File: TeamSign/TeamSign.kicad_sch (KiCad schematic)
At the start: 59 parts, among them J1 RJ45, U1 TPS563200, U2 ESP32-Devkit_C_V4

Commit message: Add SK6812-Side-A footprint/symbol to working area, as well as swapped to a stacklight connection that has a ground pin at the end for generic 12v power use.  yay!
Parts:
- L1: value L -> 3.3uH; footprint (none) -> Inductor_SMD:L_Bourns_SRN8040TA; LCSC (none) -> https://www.lcsc.com/product-detail/Power-Inductors_BOURNS-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
- R1: value 56.2kOhm -> 56.2kΩ
- R2: value 10kOhm -> 10kΩ
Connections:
- net +12V: now also J1.1
- net GND: now also J1.8
- net sk_input: now reaches U2.26 (RTC_GPIO9/XTal32P/Touch9/ADC1_4/GPIO32)
- net sk_input: now also D1.2 (DIN)
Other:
- moved on the sheet: J1
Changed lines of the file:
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@@
+    (stroke (width 0) (type default))
+  )
+  (wire (pts (xy 22.225 95.25) (xy 24.765 95.25))
     (stroke (width 0) (type default))
   )
@@
     (stroke (width 0) (type default))
   )
+  (wire (pts (xy 157.48 113.665) (xy 167.005 113.665))
+    (stroke (width 0) (type default))
+  )
   (wire (pts (xy 223.52 255.905) (xy 234.95 255.905))
     (stroke (width 0) (type default))
@@
     (stroke (width 0) (type default))
   )
+  (wire (pts (xy 22.225 113.03) (xy 24.765 113.03))
+    (stroke (width 0) (type default))
+  )
   (wire (pts (xy 264.16 255.905) (xy 275.59 255.905))
     (stroke (width 0) (type default))
@@
   )
   (wire (pts (xy 223.52 274.32) (xy 234.95 274.32))
+    (stroke (width 0) (type default))
+  )
+  (wire (pts (xy 25.4 238.125) (xy 35.56 238.125))
     (stroke (width 0) (type default))
   )
@@
     (effects (font (size 1.27 1.27)) (justify left bottom))
   )
+  (label "sk_input" (at 157.48 113.665 0) (fields_autoplaced)
+    (effects (font (size 1.27 1.27)) (justify left bottom))
+  )
+  (label "sk_input" (at 25.4 238.125 0) (fields_autoplaced)
+    (effects (font (size 1.27 1.27)) (justify left bottom))
+  )
   (symbol (lib_id "LED:SK6812") (at 214.63 266.7 0) (unit 1)
     (in_bom yes) (on_board yes) (dnp no)
@@
       (effects (font (size 1.27 1.27)) (justify left))
     )
-    (property "Value" "10kOhm" (at 81.28 66.675 0)
+    (property "Value" "10kΩ" (at 81.28 66.675 0)
       (effects (font (size 1.27 1.27)) (justify left))
     )
@@
     )
   )
-  (symbol (lib_id "Connector:RJ45") (at 30.48 107.95 0) (unit 1)
-    (in_bom yes) (on_board yes) (dnp no) (fields_autoplaced)
-    (property "Reference" "J1" (at 30.48 90.805 0)
-      (effects (font (size 1.27 1.27)))
-    )
-    (property "Value" "RJ45" (at 30.48 93.345 0)
-      (effects (font (size 1.27 1.27)))
-    )
-    (property "Footprint" "footprints:RCH RC00139" (at 30.48 107.315 90)
-      (effects (font (size 1.27 1.27)) hide)
-    )
-    (property "Datasheet" "~" (at 30.48 107.315 90)
+  (symbol (lib_id "Connector:RJ45") (at 34.925 102.87 180) (unit 1)
+    (in_bom yes) (on_board yes) (dnp no) (fields_autoplaced)
+    (property "Reference" "J1" (at 44.45 103.505 0)
+      (effects (font (size 1.27 1.27)) (justify right))
+    )
+    (property "Value" "RJ45" (at 44.45 106.045 0)
+      (effects (font (size 1.27 1.27)) (justify right))
+    )
+    (property "Footprint" "footprints:RCH RC00139" (at 34.925 103.505 90)
+      (effects (font (size 1.27 1.27)) hide)
+    )
+    (property "Datasheet" "~" (at 34.925 103.505 90)
       (effects (font (size 1.27 1.27)) hide)
     )
@@
       (effects (font (size 1.27 1.27)))
     )
-    (property "Value" "L" (at 86.36 52.705 90)
-      (effects (font (size 1.27 1.27)))
-    )
-    (property "Footprint" "" (at 86.36 54.61 0)
-      (effects (font (size 1.27 1.27)) hide)
-    )
-    (property "Datasheet" "~" (at 86.36 54.61 0)
+    (property "Value" "3.3uH" (at 86.36 52.705 90)
+      (effects (font (size 1.27 1.27)))
+    )
+    (property "Footprint" "Inductor_SMD:L_Bourns_SRN8040TA" (at 86.36 54.61 0)
+      (effects (font (size 1.27 1.27)) hide)
+    )
+    (property "Datasheet" "https://datasheet.lcsc.com/lcsc/2012151538_BOURNS-SRN8040-3R3Y_C780188.pdf" (at 86.36 54.61 0)
+      (effects (font (size 1.27 1.27)) hide)
+    )
+    (property "LCSC" "https://www.lcsc.com/product-detail/Power-Inductors_BOURNS-SRN8040-3R3Y_C780188.html" (at 86.36 54.61 90)
       (effects (font (size 1.27 1.27)) hide)
     )
@@
       (effects (font (size 1.27 1.27)) (justify left))
     )
-    (property "Value" "56.2kOhm" (at 80.01 60.96 0)
+    (property "Value" "56.2kΩ" (at 80.01 60.96 0)
       (effects (font (size 1.27 1.27)) (justify left))
     )
@@
         (path "/e53f9913-0070-41c4-b6c8-5a044462b6d9"
           (reference "D7") (unit 1)
+        )
+      )
+    )
+  )
+  (symbol (lib_id "power:+12V") (at 22.225 95.25 0) (unit 1)
+    (in_bom yes) (on_board yes) (dnp no) (fields_autoplaced)
+    (property "Reference" "#PWR010" (at 22.225 99.06 0)
+      (effects (font (size 1.27 1.27)) hide)
+    )
+    (property "Value" "+12V" (at 22.225 91.44 0)
+      (effects (font (size 1.27 1.27)))
+    )
+    (property "Footprint" "" (at 22.225 95.25 0)
+      (effects (font (size 1.27 1.27)) hide)
+    )
+    (property "Datasheet" "" (at 22.225 95.25 0)
+      (effects (font (size 1.27 1.27)) hide)
+    )
+    (pin "1")
+    (instances
+      (project "TeamSign"
+        (path "/e53f9913-0070-41c4-b6c8-5a044462b6d9"
+          (reference "#PWR010") (unit 1)
         )
       )
@@
         )
       )
+    )
+  )
+  (symbol (lib_id "power:GND") (at 22.225 113.03 0) (unit 1)
+    (in_bom yes) (on_board yes) (dnp no) (fields_autoplaced)
+    (property "Reference" "#PWR011" (at 22.225 119.38 0)
+      (effects (font (size 1.27 1.27)) hide)
+    )
+    (property "Value" "GND" (at 22.225 117.475 0)
+      (effects (font (size 1.27 1.27)))
+    )
+    (property "Footprint" "" (at 22.225 113.03 0)
+      (effects (font (size 1.27 1.27)) hide)
+    )
+    (property "Datasheet" "" (at 22.225 113.03 0)
+      (effects (font (size 1.27 1.27)) hide)
+    )
+    (pin "1")
+    (instances
+      (project "TeamSign"
+        (path "/e53f9913-0070-41c4-b6c8-5a044462b6d9"
+          (reference "#PWR011") (unit 1)
+        )
+      )

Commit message: Added subsheet for the other LEDs, still need to fix the capacitor footprint, but making solid progress it seems?  Wild!
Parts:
- removed C10, C11, C12, C13, C14, C15, C16, C17, C18, C19, C20, C21, C22, C23, C24, C25, C26, C27, C28, C4, C5, C6, C7, C8, C9: C, symbol Device:C
- removed D1, D10, D11, D12, D13, D14, D15, D16, D17, D18, D19, D2, D20, D21, D22, D23, D24, D25, D3, D4, D5, D6, D7, D8, D9: SK6812, LED_SMD:LED_SK6812_PLCC4_5.0x5.0mm_P3.2mm, symbol LED:SK6812
- added C29, C30, C31, C32, C33, C34, C35, C36: C, symbol Device:C
- added D26, D27, D28, D29, D30, D31, D32, D33: SK6812-Side-A, footprints:SK6812-Side-A, symbol symbols:SK6812_Side_A
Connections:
- net +3V3: now also C29.1, C30.1, C31.1, C32.1, C33.1, C34.1, C35.1, C36.1, D26.2 (VDD), D27.2 (VDD), D28.2 (VDD), D29.2 (VDD), D30.2 (VDD), D31.2 (VDD), D32.2 (VDD), D33.2 (VDD); no longer C3.1, L1.2, R1.1, U2.20 (3.3v)
- net GND: now also C29.2, C30.2, C31.2, C32.2, C33.2, C34.2, C35.2, C36.2, D26.4 (GND), D27.4 (GND), D28.4 (GND), D29.4 (GND), D30.4 (GND), D31.4 (GND), D32.4 (GND), D33.4 (GND)
- net stacklight_out: now reaches U2.27 (RTC_GPIO8/Xtal32N/Touch8/ADC1_5/GPIO33)
- net stacklight_out: now also D26.1 (DIN)
- net +5V: now reaches U2.38 (5V)
- net +5V: now also C3.1, L1.2, R1.1
- new net: D32.3 (DOUT), D33.1 (DIN)
- new net: D31.3 (DOUT), D32.1 (DIN)
- new net: D29.3 (DOUT), D30.1 (DIN)
- new net: D30.3 (DOUT), D31.1 (DIN)
- new net: D28.3 (DOUT), D29.1 (DIN)
- new net: D26.3 (DOUT), D27.1 (DIN)
- new net: D27.3 (DOUT), D28.1 (DIN)
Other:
- added sheet LED Array 1 (LED_Array_1.kicad_sch)
- added sheet LED Array 2 (LED_Array_1.kicad_sch)
- added sheet LED Array 3 (LED_Array_1.kicad_sch)
- note removed: "DID NO ONE ELSE SERIOUSLY WANT THIS‽"
- note removed: "MAKE SIDE FIRING SK6812 SIDE A FOOTPRINT FUCKING FUCKING FUCK!"
- note removed: "SK6812 Output (7Seg)"

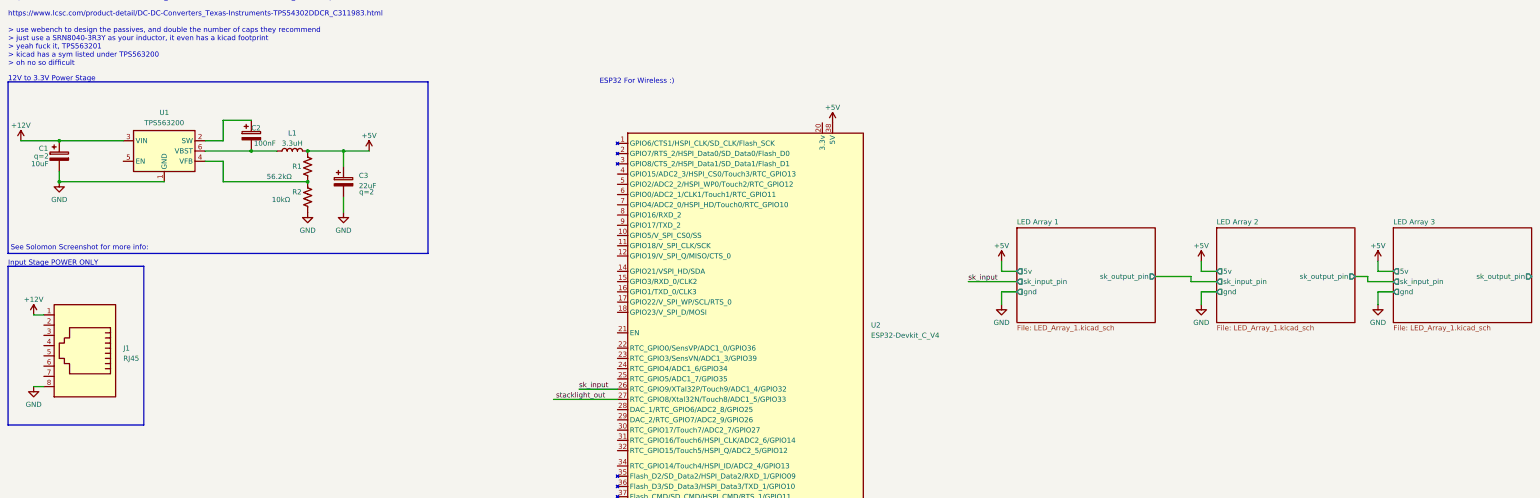
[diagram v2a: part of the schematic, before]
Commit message: Add PEM nut footprint starter to library, also did small tweaks to BOM and updated symbols to include the barrel jack antics.  Yay!
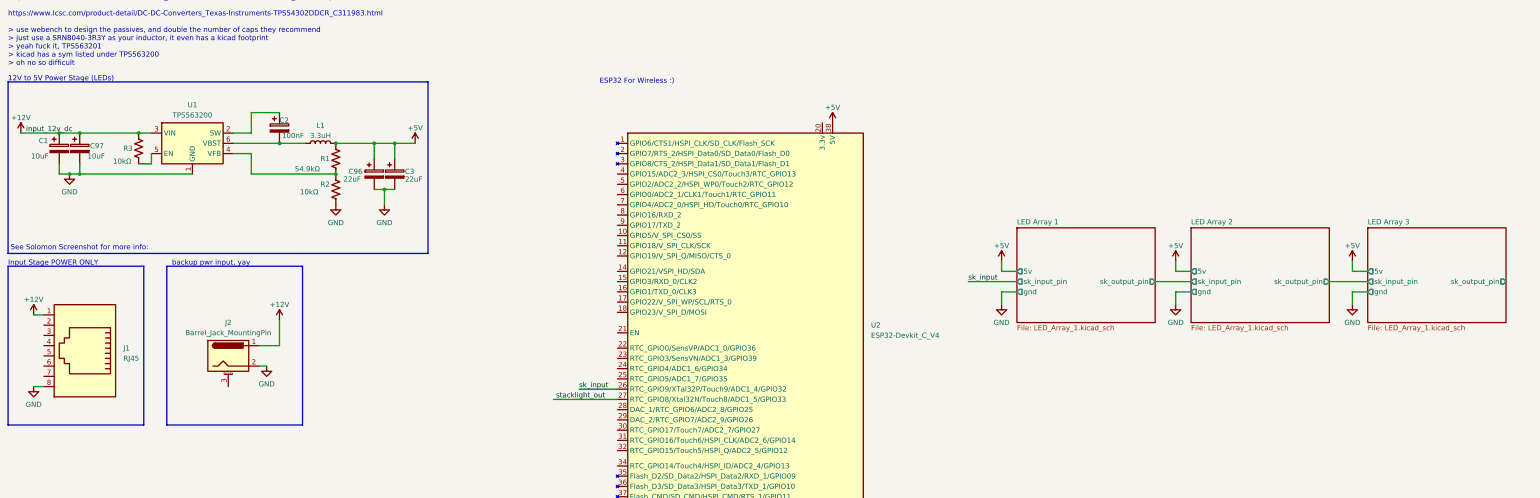
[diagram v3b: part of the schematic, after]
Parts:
- added C96: 22uF, Capacitor_SMD:CP_Elec_5x5.4, symbol Device:C_Polarized
- added C97: 10uF, Capacitor_SMD:C_1206_3216Metric_Pad1.33x1.80mm_HandSolder, symbol Device:C_Polarized
- added J2: Barrel_Jack_MountingPin, Connector_BarrelJack:BarrelJack_Horizontal, symbol symbols:Barrel_Jack_MountingPin
- added R3: 10kΩ, Resistor_SMD:R_0805_2012Metric_Pad1.20x1.40mm_HandSolder, symbol Device:R_US
- C1: footprint (none) -> Capacitor_SMD:C_1206_3216Metric_Pad1.33x1.80mm_HandSolder; LCSC (none) -> https://www.lcsc.com/product-detail/Multilayer-Ceramic-Capa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; Quantity q=2 -> (none)
- C2: footprint (none) -> Capacitor_SMD:C_1206_3216Metric_Pad1.33x1.80mm_HandSolder; LCSC (none) -> https://www.lcsc.com/product-detail/Multilayer-Ceramic-Capa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
- C3: footprint (none) -> Capacitor_SMD:CP_Elec_5x5.4; LCSC (none) -> https://www.lcsc.com/product-detail/Aluminum-Electrolytic-C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; Quantity q=2 -> (none)
- R1: value 56.2kΩ -> 54.9kΩ; footprint (none) -> Resistor_SMD:R_0805_2012Metric_Pad1.20x1.40mm_HandSolder; LCSC (none) -> https://www.lcsc.com/product-detail/Chip-Resistor-Surface-M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
- R2: footprint (none) -> Resistor_SMD:R_0805_2012Metric_Pad1.20x1.40mm_HandSolder; LCSC (none) -> https://www.lcsc.com/product-detail/Chip-Resistor-Surface-M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
- U1: Note (none) -> This is actually a TPS563201, but we're using the footprint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
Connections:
- net +12V: now also C97.1, J2.1, R3.1
- net +5V: now also C96.1
- net GND: now also C96.2, C97.2, J2.2
- net at U1.5 (EN): now also R3.2
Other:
- note added: "12V to 5V Power Stage (LEDs)"
- note added: "backup pwr input, yay"
- note removed: "12V to 3.3V Power Stage"
- moved on the sheet: C1, C2, C3, L1, R1, R2, U1

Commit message: Place caps :)
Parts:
- added C98: 100nF, Capacitor_SMD:C_1206_3216Metric_Pad1.33x1.80mm_HandSolder, symbol Device:C
- C29, C30, C31, C32, C33, C34, C35, C36: value C -> 100nF; footprint (none) -> Capacitor_SMD:C_1206_3216Metric_Pad1.33x1.80mm_HandSolder; LCSC (none) -> https://www.lcsc.com/product-detail/Multilayer-Ceramic-Capa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
- renumbered C2 to C799, C96 to C898, C3 to C899, C97 to C998, C1 to C999, D26 to D300, D27 to D301, D28 to D302, D29 to D303, D30 to D304, D31 to D305, D32 to D306, D33 to D307
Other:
- note added: "ESP32! Yay!"
- note added: "LED Arrays"
- note removed: "ESP32 For Wireless :)"
- moved on the sheet: U2

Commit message: Added gerbers for TS to the ignore, plus added level shifting.  Yay!
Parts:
- added Q1, Q2: BSS138, Package_TO_SOT_SMD:SOT-23, symbol Transistor_FET:BSS138
- added R4, R5, R6, R7: 10kΩ, Resistor_SMD:R_0805_2012Metric_Pad1.20x1.40mm_HandSolder, symbol Device:R_US
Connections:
- net +5V: now also R5.1, R7.1
- net sk_input: now also Q1.2 (S), R4.2
- net stacklight_out: now also Q2.2 (S), R6.2; no longer D300.1 (DIN)
- net +3.3V: now reaches U2.20 (3.3v)
- net +3.3V: now also Q1.1 (G), Q2.1 (G), R4.1, R6.1
- new net sk_lvl_shifted: Q1.3 (D), R5.2
- new net stacklight_lvl_shift: D300.1 (DIN), Q2.3 (D), R7.2
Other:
- note added: "Level Shifting for SK6812 Variants"
- note added: "Stacklight Emulation Mode Shit"
- moved on the sheet: C29, C30, C31, C32, C33, C34, C35, C36, C98, D300, D301, D302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

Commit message: Resolve subsheet antics... Yay.
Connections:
- net +3V3 is gone; now on net +5V: C29.1, C30.1, C31.1, C32.1, C33.1, C34.1, C35.1, C36.1, D300.2 (VDD), D301.2 (VDD), D302.2 (VDD), D303.2 (VDD), D304.2 (VDD), D305.2 (VDD), D306.2 (VDD), D307.2 (VDD)
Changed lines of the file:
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@@
-    )
-  )
-  (symbol (lib_id "power:+3V3") (at 208.28 144.145 0) (unit 1)
-    (in_bom yes) (on_board yes) (dnp no) (fields_autoplaced)
-    (property "Reference" "#PWR017" (at 208.28 147.955 0)
-      (effects (font (size 1.27 1.27)) hide)
-    )
-    (property "Value" "+3V3" (at 208.28 140.335 0)
-      (effects (font (size 1.27 1.27)))
-    )
-    (property "Footprint" "" (at 208.28 144.145 0)
-      (effects (font (size 1.27 1.27)) hide)
-    )
-    (property "Datasheet" "" (at 208.28 144.145 0)
-      (effects (font (size 1.27 1.27)) hide)
-    )
-    (pin "1")
-    (instances
-      (project "TeamSign"
-        (path "/e53f9913-0070-41c4-b6c8-5a044462b6d9"
-          (reference "#PWR017") (unit 1)
-        )
-      )
     )
   )
@@
         )
       )
+    )
+  )
+  (symbol (lib_id "power:+5V") (at 208.28 144.145 0) (unit 1)
+    (in_bom yes) (on_board yes) (dnp no) (fields_autoplaced)
+    (property "Reference" "#PWR017" (at 208.28 147.955 0)
+      (effects (font (size 1.27 1.27)) hide)
+    )
+    (property "Value" "+5V" (at 208.28 140.335 0)
+      (effects (font (size 1.27 1.27)))
+    )
+    (property "Footprint" "" (at 208.28 144.145 0)
+      (effects (font (size 1.27 1.27)) hide)
+    )
+    (property "Datasheet" "" (at 208.28 144.145 0)
+      (effects (font (size 1.27 1.27)) hide)
+    )
+    (pin "1")
+    (instances
+      (project "TeamSign"
+        (path "/e53f9913-0070-41c4-b6c8-5a044462b6d9"
+          (reference "#PWR017") (unit 1)
+        )
+      )

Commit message: Added power area, and started drawing pours.
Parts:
- added C87, C90, C93, C96: 100nF, Capacitor_SMD:C_1206_3216Metric_Pad1.33x1.80mm_HandSolder, symbol Device:C
- added D29, D30, D31, D32: SK6812, LED_SMD:LED_SK6812_PLCC4_5.0x5.0mm_P3.2mm, symbol LED:SK6812
- added H1, H2, H3, H4: MountingHole, MountingHole:MountingHole_3.2mm_M3, symbol Mechanical:MountingHole
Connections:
- net +5V: now also C87.1, C90.1, C93.1, C96.1, D29.3 (VDD), D30.3 (VDD), D31.3 (VDD), D32.3 (VDD)
- net GND: now also C87.2, C90.2, C93.2, C96.2, D29.1 (VSS), D30.1 (VSS), D31.1 (VSS), D32.1 (VSS)
- net sk_input: now also U2.27 (RTC_GPIO8/Xtal32N/Touch8/ADC1_5/GPIO33); no longer U2.26 (RTC_GPIO9/XTal32P/Touch9/ADC1_4/GPIO32)
- net stacklight_out: now also U2.26 (RTC_GPIO9/XTal32P/Touch9/ADC1_4/GPIO32); no longer U2.27 (RTC_GPIO8/Xtal32N/Touch8/ADC1_5/GPIO33)
- new net: D29.4 (DOUT), D30.2 (DIN)
- new net: D30.4 (DOUT), D31.2 (DIN)
- new net: D31.4 (DOUT), D32.2 (DIN)
- new net led_output_frontfiring: D29.2 (DIN)
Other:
- note added: "Extra LEDs! (Up-firing)"
- note added: "Mounting Points (M2.5/M3/need washers)"
- moved on the sheet: C98
